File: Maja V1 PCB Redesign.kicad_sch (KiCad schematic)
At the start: 21 parts, among them J1 TYPE-C-31-M-12, J2 AVR-ISP-6, U1 ATmega32U4-M, U2 PRTR5V0U2X, Y1 Crystal_GND24_Small

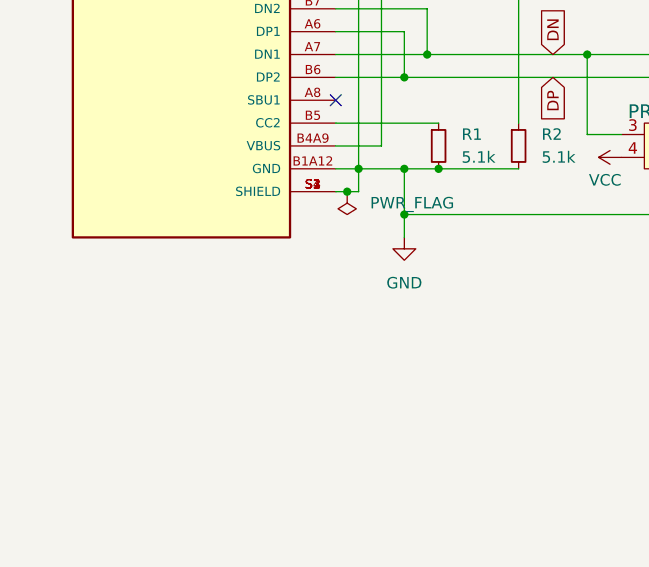
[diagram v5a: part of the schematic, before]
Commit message: add farret
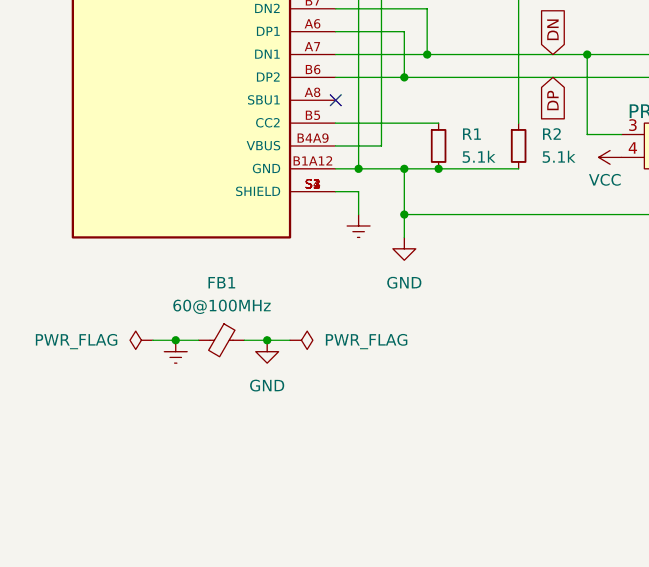
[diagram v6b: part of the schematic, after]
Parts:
- added FB1: 60@100MHz, Inductor_SMD:L_0805_2012Metric_Pad1.15x1.40mm_HandSolder, symbol Device:FerriteBead_Small
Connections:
- net GND: now also FB1.1; no longer J1.S1 (SHIELD), J1.S2 (SHIELD), J1.S3 (SHIELD), J1.S4 (SHIELD)
- new net Earth: FB1.2, J1.S1 (SHIELD), J1.S2 (SHIELD), J1.S3 (SHIELD), J1.S4 (SHIELD)
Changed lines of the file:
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@@
   (junction (at 100.33 101.6) (diameter 0) (color 0 0 0 0)
   )
+  (junction (at 35.56 130.81) (diameter 0) (color 0 0 0 0)
+  )
   (junction (at 55.88 111.76) (diameter 0) (color 0 0 0 0)
   )
@@
   (junction (at 60.96 111.76) (diameter 0) (color 0 0 0 0)
   )
+  (junction (at 45.72 130.81) (diameter 0) (color 0 0 0 0)
+  )
   (junction (at 257.81 134.62) (diameter 0) (color 0 0 0 0)
   )
@@
   )
   (junction (at 63.5 86.36) (diameter 0) (color 0 0 0 0)
-  )
-  (junction (at 54.61 114.3) (diameter 0) (color 0 0 0 0)
   )
   (junction (at 247.65 88.9) (diameter 0) (color 0 0 0 0)
@@
     (stroke (width 0) (type default) (color 0 0 0 0))
   )
-  (wire (pts (xy 54.61 114.3) (xy 55.88 114.3))
-    (stroke (width 0) (type default) (color 0 0 0 0))
-  )
   (wire (pts (xy 58.42 109.22) (xy 58.42 86.36))
     (stroke (width 0) (type default) (color 0 0 0 0))
@@
     (stroke (width 0) (type default) (color 0 0 0 0))
   )
-  (wire (pts (xy 53.34 114.3) (xy 54.61 114.3))
-    (stroke (width 0) (type default) (color 0 0 0 0))
-  )
   (wire (pts (xy 175.26 101.6) (xy 177.8 101.6))
     (stroke (width 0) (type default) (color 0 0 0 0))
@@
     (stroke (width 0) (type default) (color 0 0 0 0))
   )
-  (wire (pts (xy 55.88 114.3) (xy 55.88 111.76))
-    (stroke (width 0) (type default) (color 0 0 0 0))
-  )
   (wire (pts (xy 137.16 91.44) (xy 144.78 91.44))
     (stroke (width 0) (type default) (color 0 0 0 0))
   )
+  (wire (pts (xy 45.72 130.81) (xy 48.26 130.81))
+    (stroke (width 0) (type default) (color 0 0 0 0))
+  )
   (wire (pts (xy 100.33 101.6) (xy 102.87 101.6))
     (stroke (width 0) (type default) (color 0 0 0 0))
   )
+  (wire (pts (xy 43.18 130.81) (xy 45.72 130.81))
+    (stroke (width 0) (type default) (color 0 0 0 0))
+  )
+  (wire (pts (xy 35.56 130.81) (xy 38.1 130.81))
+    (stroke (width 0) (type default) (color 0 0 0 0))
+  )
   (wire (pts (xy 82.55 25.4) (xy 82.55 26.67))
     (stroke (width 0) (type default) (color 0 0 0 0))
@@
     (stroke (width 0) (type default) (color 0 0 0 0))
   )
+  (wire (pts (xy 53.34 114.3) (xy 55.88 114.3))
+    (stroke (width 0) (type default) (color 0 0 0 0))
+  )
   (wire (pts (xy 72.39 86.36) (xy 74.93 86.36))
     (stroke (width 0) (type default) (color 0 0 0 0))
   )
+  (wire (pts (xy 33.02 130.81) (xy 35.56 130.81))
+    (stroke (width 0) (type default) (color 0 0 0 0))
+  )
   (wire (pts (xy 53.34 99.06) (xy 63.5 99.06))
     (stroke (width 0) (type default) (color 0 0 0 0))
@@
   )
   (wire (pts (xy 175.26 129.54) (xy 179.07 129.54))
+    (stroke (width 0) (type default) (color 0 0 0 0))
+  )
+  (wire (pts (xy 55.88 114.3) (xy 55.88 116.84))
     (stroke (width 0) (type default) (color 0 0 0 0))
   )
@@
     )
   )
-  (symbol (lib_id "power:PWR_FLAG") (at 54.61 114.3 180) (unit 1)
-    (in_bom yes) (on_board yes) (fields_autoplaced)
-    (property "Reference" "#FLG0101" (id 0) (at 54.61 116.205 0)
-      (effects (font (size 1.27 1.27)) hide)
-    )
-    (property "Value" "PWR_FLAG" (id 1) (at 57.15 115.5699 0)
-      (effects (font (size 1.27 1.27)) (justify right))
-    )
-    (property "Footprint" "" (id 2) (at 54.61 114.3 0)
-      (effects (font (size 1.27 1.27)) hide)
-    )
-    (property "Datasheet" "~" (id 3) (at 54.61 114.3 0)
+  (symbol (lib_id "power:PWR_FLAG") (at 33.02 130.81 90) (unit 1)
+    (in_bom yes) (on_board yes) (fields_autoplaced)
+    (property "Reference" "#FLG0101" (id 0) (at 31.115 130.81 0)
+      (effects (font (size 1.27 1.27)) hide)
+    )
+    (property "Value" "PWR_FLAG" (id 1) (at 29.21 130.8099 90)
+      (effects (font (size 1.27 1.27)) (justify left))
+    )
+    (property "Footprint" "" (id 2) (at 33.02 130.81 0)
+      (effects (font (size 1.27 1.27)) hide)
+    )
+    (property "Datasheet" "~" (id 3) (at 33.02 130.81 0)
+      (effects (font (size 1.27 1.27)) hide)
+    )
+    (pin "1")
+  )
+  (symbol (lib_id "power:Earth") (at 35.56 130.81 0) (unit 1)
+    (in_bom yes) (on_board yes) (fields_autoplaced)
+    (property "Reference" "#PWR0118" (id 0) (at 35.56 137.16 0)
+      (effects (font (size 1.27 1.27)) hide)
+    )
+    (property "Value" "Earth" (id 1) (at 35.56 134.62 0)
+      (effects (font (size 1.27 1.27)) hide)
+    )
+    (property "Footprint" "" (id 2) (at 35.56 130.81 0)
+      (effects (font (size 1.27 1.27)) hide)
+    )
+    (property "Datasheet" "~" (id 3) (at 35.56 130.81 0)
       (effects (font (size 1.27 1.27)) hide)
     )
@@
     (pin "1")
     (pin "2")
+  )
+  (symbol (lib_id "power:Earth") (at 55.88 116.84 0) (unit 1)
+    (in_bom yes) (on_board yes) (fields_autoplaced)
+    (property "Reference" "#PWR0117" (id 0) (at 55.88 123.19 0)
+      (effects (font (size 1.27 1.27)) hide)
+    )
+    (property "Value" "Earth" (id 1) (at 55.88 120.65 0)
+      (effects (font (size 1.27 1.27)) hide)
+    )
+    (property "Footprint" "" (id 2) (at 55.88 116.84 0)
+      (effects (font (size 1.27 1.27)) hide)
+    )
+    (property "Datasheet" "~" (id 3) (at 55.88 116.84 0)
+      (effects (font (size 1.27 1.27)) hide)
+    )
+    (pin "1")
   )
   (symbol (lib_id "power:+5V") (at 207.01 17.78 0) (unit 1)
@@
     (pin "1")
   )
+  (symbol (lib_id "Device:FerriteBead_Small") (at 40.64 130.81 270) (unit 1)
+    (in_bom yes) (on_board yes) (fields_autoplaced)
+    (property "Reference" "FB1" (id 0) (at 40.6781 124.46 90))
+    (property "Value" "60@100MHz" (id 1) (at 40.6781 127 90))
+    (property "Footprint" "Inductor_SMD:L_0805_2012Metric_Pad1.15x1.40mm_HandSolder" (id 2) (at 40.64 129.032 90)
+      (effects (font (size 1.27 1.27)) hide)
+    )
+    (property "Datasheet" "~" (id 3) (at 40.64 130.81 0)
+      (effects (font (size 1.27 1.27)) hide)
+    )
+    (property "LCSC" "" (id 4) (at 40.64 130.81 90)
+      (effects (font (size 1.27 1.27)) hide)
+    )
+    (pin "1")
+    (pin "2")
+  )
   (symbol (lib_id "SKQGAFE010:SKQGAFE010") (at 71.12 36.83 0) (unit 1)
     (in_bom yes) (on_board yes) (fields_autoplaced)
@@
     )
     (property "Datasheet" "" (id 3) (at 137.16 96.52 0)
+      (effects (font (size 1.27 1.27)) hide)
+    )
+    (pin "1")
+  )
+  (symbol (lib_id "power:PWR_FLAG") (at 48.26 130.81 270) (unit 1)
+    (in_bom yes) (on_board yes) (fields_autoplaced)
+    (property "Reference" "#FLG0104" (id 0) (at 50.165 130.81 0)
+      (effects (font (size 1.27 1.27)) hide)
+    )
+    (property "Value" "PWR_FLAG" (id 1) (at 52.07 130.8099 90)
+      (effects (font (size 1.27 1.27)) (justify left))
+    )
+    (property "Footprint" "" (id 2) (at 48.26 130.81 0)
+      (effects (font (size 1.27 1.27)) hide)
+    )
+    (property "Datasheet" "~" (id 3) (at 48.26 130.81 0)
+      (effects (font (size 1.27 1.27)) hide)
+    )
+    (pin "1")
+  )
+  (symbol (lib_id "power:GND") (at 45.72 130.81 0) (unit 1)
+    (in_bom yes) (on_board yes) (fields_autoplaced)
+    (property "Reference" "#PWR0119" (id 0) (at 45.72 137.16 0)
+      (effects (font (size 1.27 1.27)) hide)
+    )
+    (property "Value" "GND" (id 1) (at 45.72 135.89 0))
+    (property "Footprint" "" (id 2) (at 45.72 130.81 0)
+      (effects (font (size 1.27 1.27)) hide)
+    )
+    (property "Datasheet" "" (id 3) (at 45.72 130.81 0)
       (effects (font (size 1.27 1.27)) hide)
     )
@@
       (reference "#FLG0103") (unit 1) (value "PWR_FLAG") (footprint "")
     )
+    (path "/bd3db677-9d0f-46c1-9956-a17efb62c6d3"
+      (reference "#FLG0104") (unit 1) (value "PWR_FLAG") (footprint "")
+    )
     (path "/69708766-0768-4b9c-83fc-cfa31b57c63a"
       (reference "#PWR0101") (unit 1) (value "GND") (footprint "")
@@
       (reference "#PWR0116") (unit 1) (value "+5V") (footprint "")
     )
+    (path "/3b72bf1b-6bb2-476a-a8a6-d9ee84fe0b50"
+      (reference "#PWR0117") (unit 1) (value "Earth") (footprint "")
+    )
+    (path "/104d142c-2848-43a9-90f7-418cfe11ef1c"
+      (reference "#PWR0118") (unit 1) (value "Earth") (footprint "")
+    )
+    (path "/bd716238-6a87-484f-bf5b-0fbed543ac82"
+      (reference "#PWR0119") (unit 1) (value "GND") (footprint "")
+    )
     (path "/43d87709-5a30-4180-96d5-6f8b8ffdfd1d"
       (reference "C1") (unit 1) (value "1u") (footprint "Capacitor_SMD:C_0805_2012Metric_Pad1.18x1.45mm_HandSolder")
@@
       (reference "F1") (unit 1) (value "500m") (footprint "Fuse:Fuse_1206_3216Metric_Pad1.42x1.75mm_HandSolder")
     )
+    (path "/838a9ece-0241-4a45-a7ad-d6562d321675"
+      (reference "FB1") (unit 1) (value "60@100MHz") (footprint "Inductor_SMD:L_0805_2012Metric_Pad1.15x1.40mm_HandSolder")
+    )
     (path "/31ab6056-77a7-4722-90c3-619f8073b0cc"
